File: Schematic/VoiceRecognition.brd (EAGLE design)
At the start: 26 parts, among them Q1 16MHz, X1 USB-A

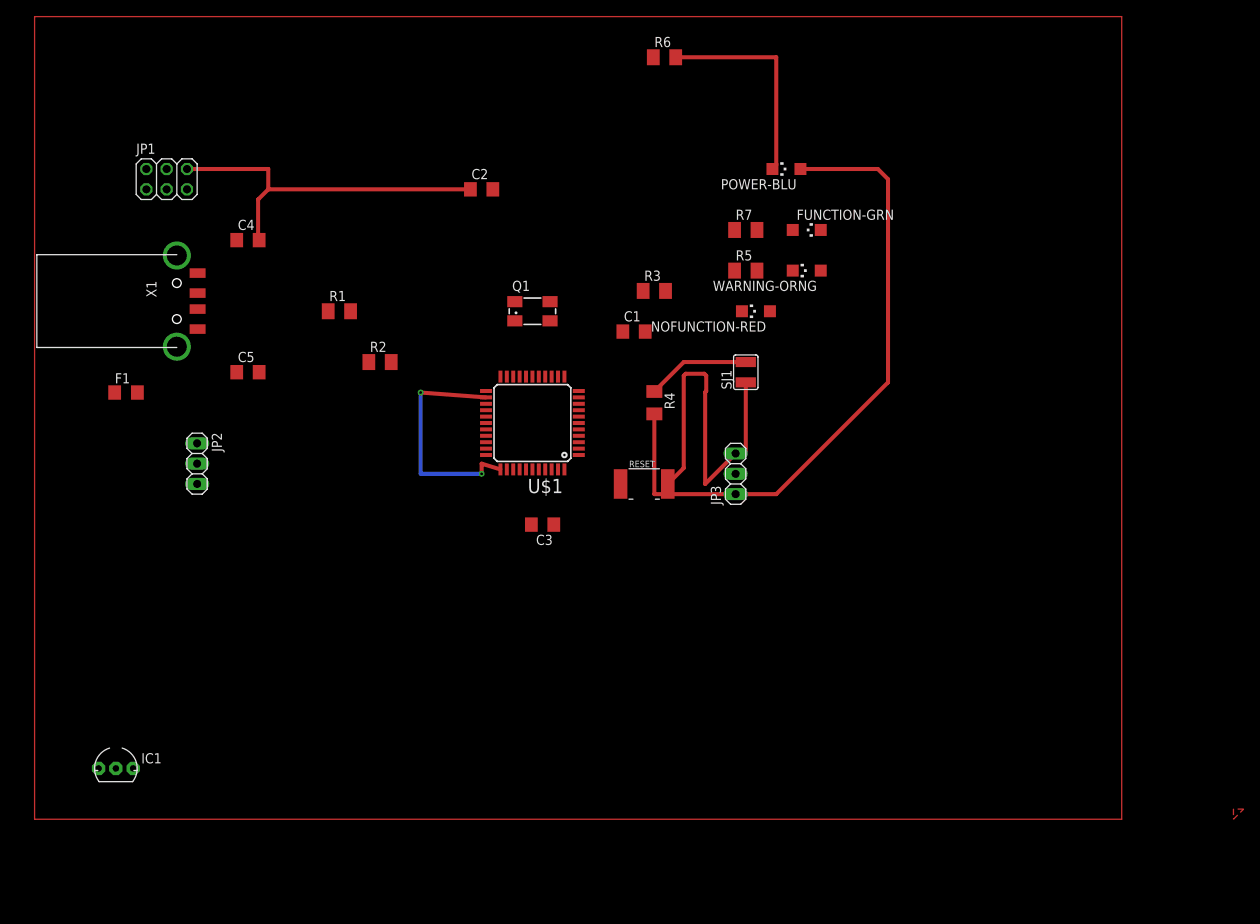
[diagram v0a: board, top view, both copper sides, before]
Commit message: Added some EagleCAD schematic updates
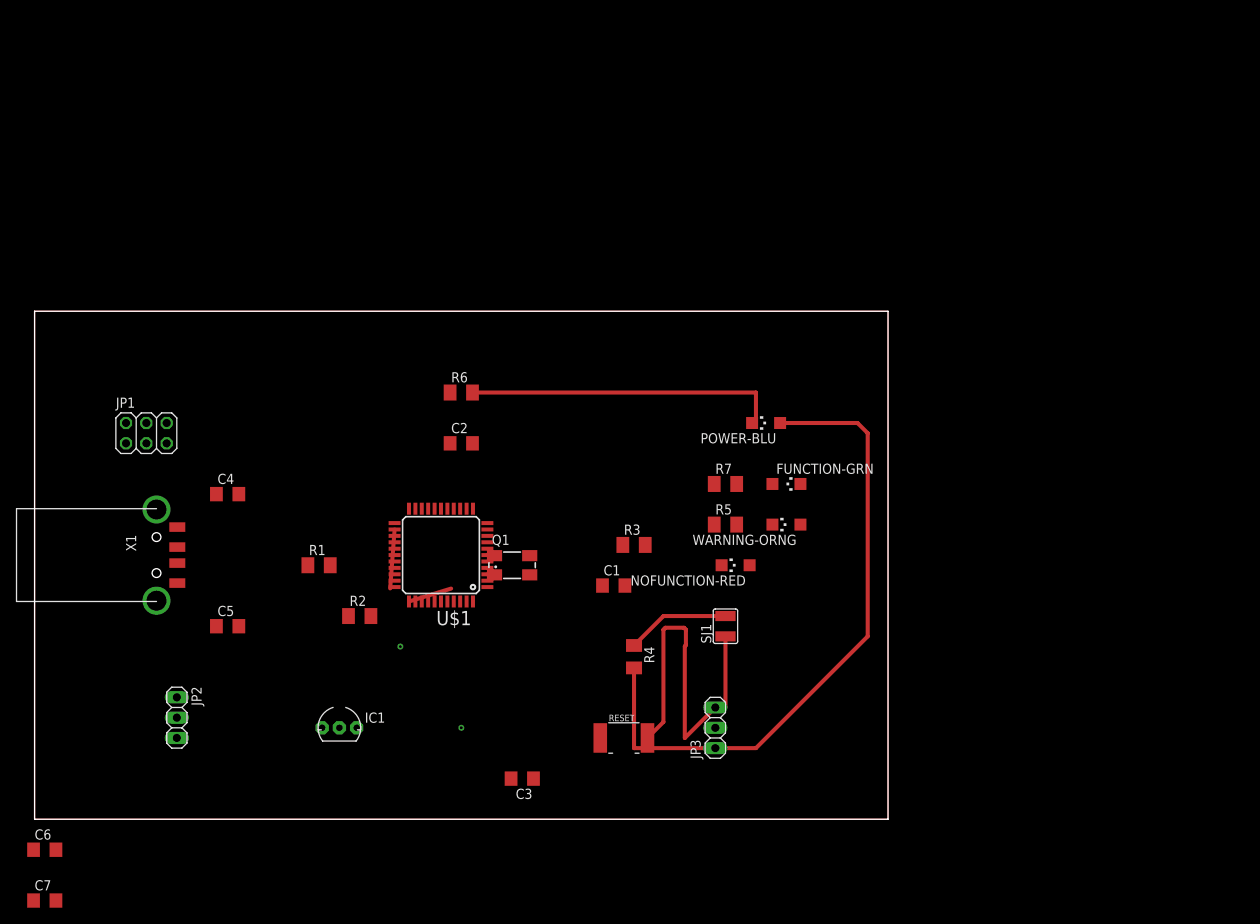
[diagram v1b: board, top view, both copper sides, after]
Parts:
- removed F1: (no value), adafruit:R1206
- added C6, C7: 1uF, rcl:C1206
- moved R6 49.0 mm to (53.3, 53.3)
- moved JP1 31.9 mm to (14.0, 48.3)
- moved R3 31.9 mm to (74.9, 34.3)
- moved C5 31.9 mm to (24.1, 24.1)
- moved JP2 31.9 mm to (17.8, 12.7)
- moved SJ1 31.9 mm to (86.4, 24.1)
- moved C1 31.9 mm to (72.4, 29.2)
- moved C3 31.9 mm to (61.0, 5.08)
- moved C4 31.9 mm to (24.1, 40.6)
- moved FUNCTION-GRN 31.9 mm to (94.0, 41.9)
- moved JP3 31.9 mm to (85.1, 11.4)
- moved NOFUNCTION-RED 31.9 mm to (87.6, 31.8)
- moved POWER-BLU 31.9 mm to (91.4, 49.5)
- moved Q1 31.9 mm to (59.7, 31.8)
- moved R1 31.9 mm to (35.6, 31.8)
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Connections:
- net GND: now also C6.2, C7.2, IC1.1
- net N$10: now also C6.1, IC1.2; no longer F1.1
- net VCC: now also C7.1, IC1.3; no longer F1.2
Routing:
- net N$18: track 472.4 -> 340.4 mm
- net GND: track 91.4 -> 46.7 mm
- net VCC: track 111.6 -> 94.8 mm
- net N$5: track 26.7 -> 39.4 mm
- removed copper zone on layer 1, net N$14
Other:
- board outline added: 106.7 x 63.5 mm
